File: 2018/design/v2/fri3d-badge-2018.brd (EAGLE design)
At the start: 80 x 60 mm, 138 parts

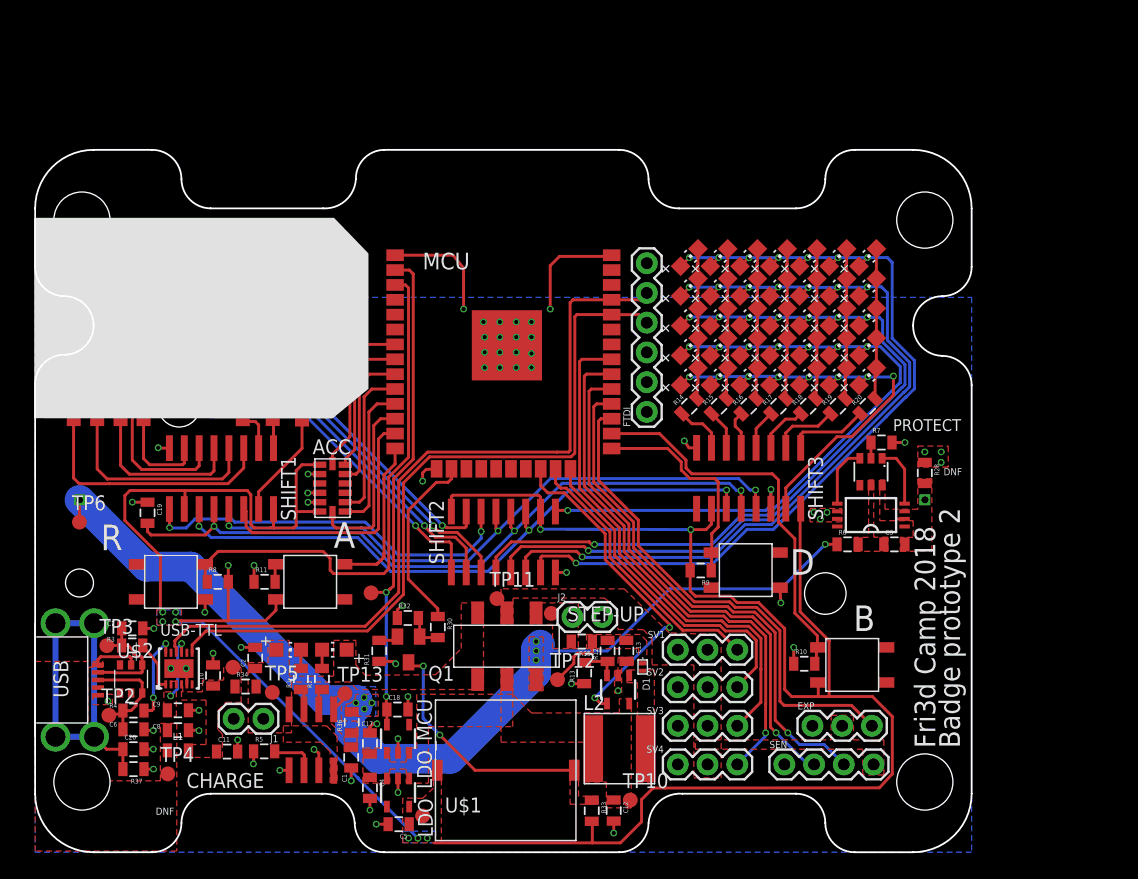
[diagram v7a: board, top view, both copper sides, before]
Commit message: redid USB entry/ESD + cleaned up silk
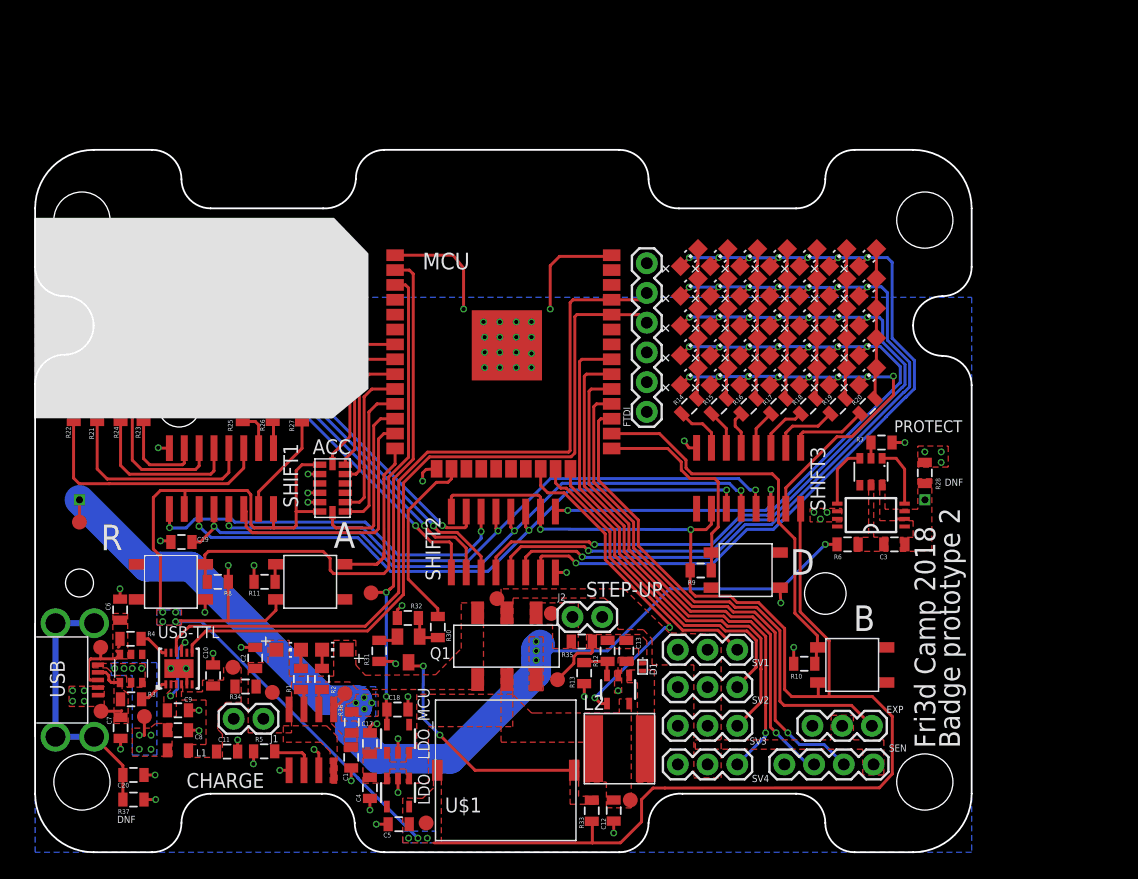
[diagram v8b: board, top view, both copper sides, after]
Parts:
- moved C6 10.3 mm to (7.26, 20.7), turned to 90 degrees
- moved C7 8.56 mm to (7.30, 10.6), turned to 270 degrees
- moved R4 6.14 mm to (8.15, 18.2)
- moved TP2 5.84 mm to (5.60, 17.5)
- moved TP3 5.62 mm to (5.63, 12.0)
- moved TP4 5.29 mm to (9.34, 11.6)
- moved R3 4.60 mm to (8.20, 13.1)
- moved C19 3.83 mm to (12.5, 26.5), turned to 0 degrees
- moved R37 2.60 mm to (8.40, 4.50)
- moved C20 2.20 mm to (8.40, 6.60)
- moved U$2 0.90 mm to (8.20, 15.7), turned to 180 degrees
- moved TP8 0.67 mm to (33.4, 2.50)
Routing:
- net N$23: track 30.6 -> 22.7 mm
- net D-: track 10.1 -> 4.58 mm
- net N$5: track 7.67 -> 2.60 mm, vias 2 -> 0
- net LEDS_RCK: track 61.3 -> 57.0 mm
- net D+: track 10.6 -> 6.81 mm
- net 3V3: track 210.1 -> 206.6 mm
- net USB-RAW: track 4.20 -> 2.21 mm, vias 0 -> 8
- net N$3: track 4.40 -> 2.59 mm
- net VBAT: track 87.6 -> 88.5 mm
- net RESET: track 45.2 -> 45.7 mm
- net GND: track 65.7 -> 65.8 mm, vias 64 -> 67
- added copper zone on layer 1, net D+
- added copper zone on layer 1, net D-
- added copper zone on layer 16, net USB-RAW
